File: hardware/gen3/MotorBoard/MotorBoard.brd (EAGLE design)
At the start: 140 x 100 mm, 273 parts, among them M10O1 TEST_PT, M1O2 TEST_PT, M1O3 TEST_PT, M2O1 TEST_PT, M2O2 TEST_PT, M2O3 TEST_PT, M3O1 TEST_PT, M3O2 TEST_PT, M3O3 TEST_PT, M4O1 TEST_PT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

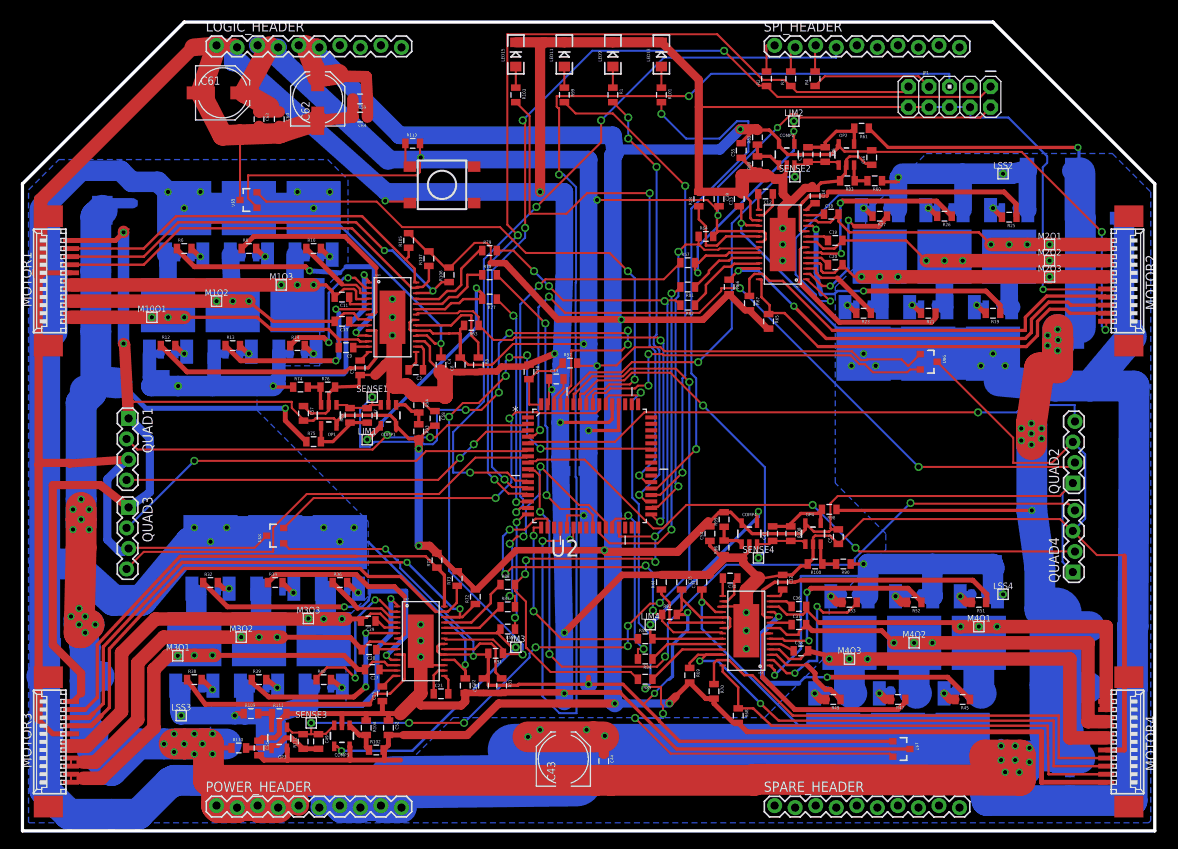
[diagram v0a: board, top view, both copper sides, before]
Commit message: DRC fixes for mtor
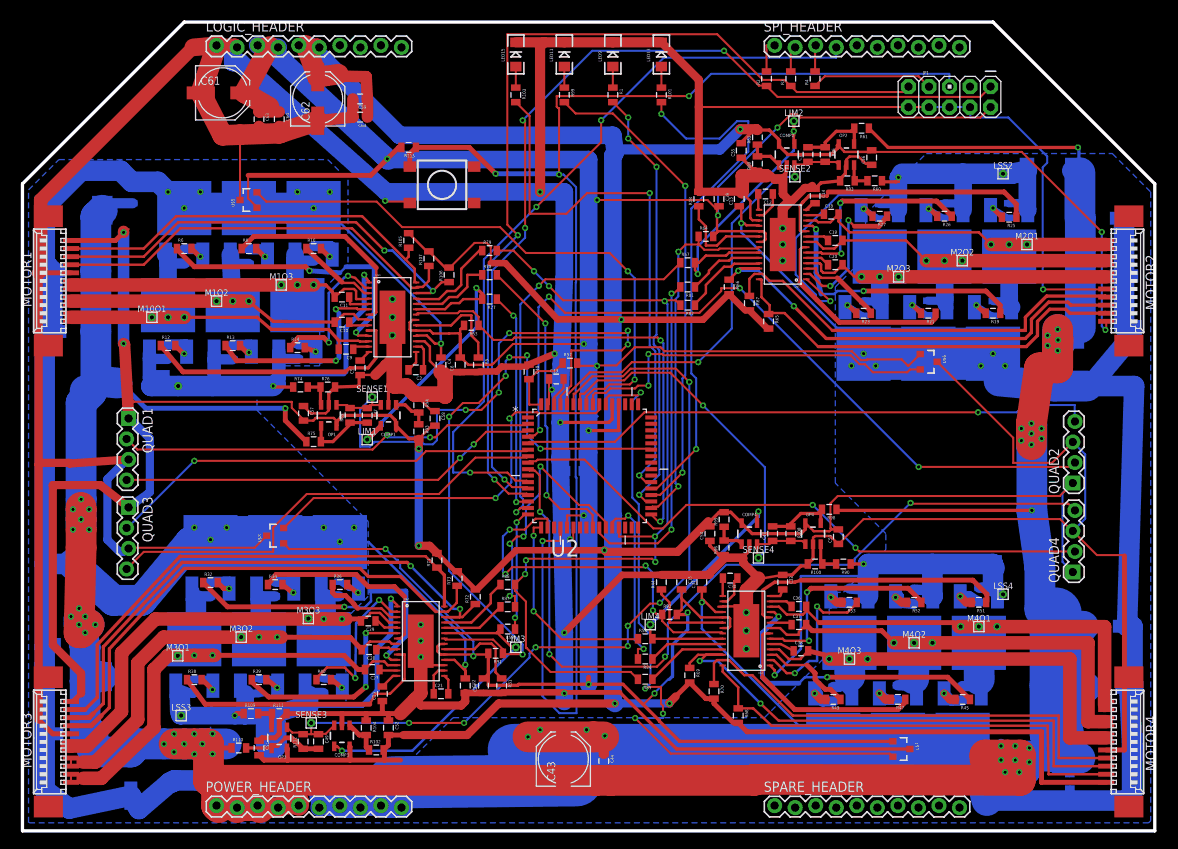
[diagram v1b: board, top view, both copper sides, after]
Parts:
- moved M2O3 18.7 mm to (108.3, 68.5)
- moved M2O2 10.8 mm to (116.2, 70.5)
- moved C50 3.32 mm to (13.4, 7.05)
- moved M2O1 2.79 mm to (124.2, 72.5)
- moved C25 0.75 mm to (133.9, 25.3)
- moved R113 0.71 mm to (47.8, 84.5), turned to 180 degrees
- moved D2 0.65 mm to (130.1, 13.5)
- moved R11 0.40 mm to (36.0, 71.4), turned to 270 degrees
- moved R20 0.40 mm to (120.0, 64.6), turned to 90 degrees
- moved R24 0.40 mm to (104.0, 64.6), turned to 90 degrees
- moved R30 0.40 mm to (106.0, 76.6), turned to 90 degrees
- moved R22 0.35 mm to (112.0, 64.7), turned to 90 degrees
- moved R50 0.35 mm to (100.2, 16.9), turned to 90 degrees
- moved C42 0.35 mm to (134.2, 17.8)
- moved D3 0.30 mm to (9.80, 15.9)
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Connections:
- removed net RESET1: R113.1, S1.A2
- net RESET: now also R113.1, S1.A2
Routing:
- net RESET: track 157.2 -> 179.5 mm, vias 3 -> 4
- net 12VGND: track 474.6 -> 487.3 mm, vias 22 -> 41
- net 12V: track 620.0 -> 629.8 mm, vias 9 -> 22
- net O2: track 67.8 -> 72.4 mm
- net 3.3V: track 451.7 -> 447.3 mm
- net O4: track 58.2 -> 61.7 mm
- net N$57: track 4.82 -> 8.30 mm
- net RESET1: track 3.42 -> 0.00 mm
- net O1: track 67.3 -> 70.4 mm
- net N$79: track 4.12 -> 6.61 mm
- net O3: track 57.8 -> 60.2 mm
- net N$80: track 4.12 -> 6.36 mm
- net M4O1: track 66.8 -> 68.7 mm
- net N$54: track 4.76 -> 6.51 mm
- net N$55: track 3.89 -> 5.38 mm
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
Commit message: fixed all DRC. vias in pads are ok, right?
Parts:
- moved LSS4 5.66 mm to (117.2, 33.2)
- renumbered M10O1 to M1O1
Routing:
- net O4: track 61.7 -> 66.3 mm
- net 12V: track 629.8 -> 634.0 mm, vias 22 -> 26
- net GND: track 857.2 -> 859.4 mm, vias 16 -> 17
- net 12VGND: track 487.3 -> 489.1 mm, vias 41 -> 44
- net RESET: track 179.5 -> 181.1 mm
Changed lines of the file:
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@@
 <setting verticaltext="up"/>
 </settings>
-<grid distance="0.05" unitdist="mm" unit="mm" style="lines" multiple="1" display="yes" altdistance="0.005" altunitdist="inch" altunit="inch"/>
+<grid distance="1" unitdist="mm" unit="mm" style="lines" multiple="1" display="yes" altdistance="0.005" altunitdist="inch" altunit="inch"/>
 <layers>
-<layer number="1" name="Top" color="4" fill="1" visible="no" active="yes"/>
+<layer number="1" name="Top" color="4" fill="1" visible="yes" active="yes"/>
 <layer number="2" name="Route2" color="1" fill="3" visible="no" active="no"/>
 <layer number="3" name="Route3" color="4" fill="3" visible="no" active="no"/>
@@
 </class>
 </classes>
-<designrules name="default">
+<designrules name="default *">
 <description language="de">&lt;b&gt;EAGLE Design Rules&lt;/b&gt;
 &lt;p&gt;
@@
 <param name="mdSmdStop" value="0mil"/>
 <param name="msWidth" value="10mil"/>
-<param name="msDrill" value="24mil"/>
+<param name="msDrill" value="15mil"/>
 <param name="msMicroVia" value="9.99mm"/>
 <param name="msBlindViaRatio" value="0.5"/>
@@
 <element name="LSS1" library="gen3" package="TESTING_PT" value="TEST_PT" x="19.25" y="55" rot="MR0"/>
 <element name="LSS2" library="gen3" package="TESTING_PT" value="TEST_PT" x="121.25" y="81.25"/>
-<element name="LSS4" library="gen3" package="TESTING_PT" value="TEST_PT" x="121.25" y="29.25"/>
+<element name="LSS4" library="gen3" package="TESTING_PT" value="TEST_PT" x="117.25" y="33.25"/>
 <element name="LSS3" library="gen3" package="TESTING_PT" value="TEST_PT" x="19.625" y="14.25"/>
 <element name="M3O3" library="gen3" package="TESTING_PT" value="TEST_PT" x="35.35" y="26.25"/>
@@
 <element name="M2O2" library="gen3" package="TESTING_PT" value="TEST_PT" x="116.205" y="70.5"/>
 <element name="M2O3" library="gen3" package="TESTING_PT" value="TEST_PT" x="108.331" y="68.5"/>
-<element name="M10O1" library="gen3" package="TESTING_PT" value="TEST_PT" x="16" y="63.5"/>
+<element name="M1O1" library="gen3" package="TESTING_PT" value="TEST_PT" x="16" y="63.5"/>
 <element name="M1O2" library="gen3" package="TESTING_PT" value="TEST_PT" x="24" y="65.5"/>
 <element name="M1O3" library="gen3" package="TESTING_PT" value="TEST_PT" x="32" y="67.5"/>
@@
 <wire x1="21.123" y1="96.873" x2="2.25" y2="78" width="1.6764" layer="1"/>
 <wire x1="2.25" y1="78" x2="2.25" y2="69.25" width="1.6764" layer="1"/>
-<wire x1="2.25" y1="69.25" x2="2" y2="69" width="1.6764" layer="1"/>
+<wire x1="2.25" y1="69.25" x2="2" y2="69" width="1.4224" layer="1"/>
 <wire x1="49.25" y1="23.455" x2="49.25" y2="21.5" width="1.6764" layer="1"/>
 <wire x1="49.25" y1="21.5" x2="49.25" y2="20.5" width="1.6764" layer="1"/>
@@
 <wire x1="26.55" y1="96.9" x2="26.54" y2="96.873" width="0.254" layer="16"/>
 <wire x1="26.55" y1="96.9" x2="26" y2="96.333" width="0.254" layer="16"/>
+<via x="45.75" y="65.75" extent="1-16" drill="0.508"/>
+<wire x1="45.75" y1="65.75" x2="45.75" y2="63.5" width="1.27" layer="1"/>
 </signal>
 <signal name="3.3V">
@@
 <wire x1="47.9" y1="82.15" x2="47.9" y2="83.75" width="0.609" layer="1"/>
 <wire x1="47.9" y1="83.75" x2="48.65" y2="84.5" width="0.609" layer="1"/>
-<wire x1="48.65" y1="84.5" x2="55.25" y2="84.5" width="0.609" layer="1"/>
-<wire x1="55.25" y1="84.5" x2="58.5" y2="81.25" width="0.609" layer="1"/>
+<wire x1="48.65" y1="84.5" x2="58.25" y2="84.5" width="0.609" layer="1"/>
+<wire x1="58.25" y1="84.5" x2="58.5" y2="81.25" width="0.609" layer="1"/>
 <via x="58.5" y="81.25" extent="1-16" drill="0.381" diameter="0.508"/>
 <wire x1="58.5" y1="81.25" x2="66.25" y2="81.25" width="0.609" layer="16"/>
@@
 <via x="69.75" y="12.5" extent="1-16" drill="0.381" diameter="0.508"/>
 <via x="72" y="11.75" extent="1-16" drill="0.381" diameter="0.508"/>
-<wire x1="20" y1="77" x2="22" y2="79" width="0" layer="19" extent="16-16"/>
-<wire x1="72" y1="11.75" x2="71.875" y2="11.625" width="0" layer="19" extent="1-1"/>
+<via x="102.5" y="57.5" extent="1-16" drill="0.381"/>
+<via x="105.5" y="57.5" extent="1-16" drill="0.381"/>
+<wire x1="105.5" y1="57.5" x2="104" y2="59" width="1.27" layer="16"/>
+<wire x1="102.5" y1="57.5" x2="104" y2="59" width="1.27" layer="16"/>
+<via x="118.5" y="57.5" extent="1-16" drill="0.381"/>
+<via x="121.5" y="57.5" extent="1-16" drill="0.381"/>
+<wire x1="120.5" y1="58.5" x2="121.5" y2="57.5" width="0" layer="19" extent="16-16"/>
 <wire x1="18" y1="79" x2="16.75" y2="80.25" width="0" layer="19" extent="16-16"/>
+<wire x1="118.5" y1="57.5" x2="120" y2="59" width="0" layer="19" extent="16-16"/>
 <wire x1="41" y1="37.5" x2="39.25" y2="35.75" width="0" layer="19" extent="1-1"/>
 <wire x1="37.25" y1="37.5" x2="39.25" y2="35.75" width="0" layer="19" extent="1-1"/>
+<wire x1="22" y1="79" x2="20" y2="77" width="0" layer="19" extent="16-16"/>
 </signal>
 <signal name="12VGND">
@@
 <wire x1="31.874" y1="3.127" x2="31.62" y2="2.873" width="2.1844" layer="1"/>
 <wire x1="31.62" y1="2.873" x2="29.334" y2="2.873" width="2.54" layer="1"/>
-<wire x1="29.334" y1="2.873" x2="29.08" y2="3.127" width="3.81" layer="1"/>
-<wire x1="29.08" y1="3.127" x2="26.794" y2="3.127" width="3.81" layer="1"/>
-<wire x1="26.794" y1="3.127" x2="26.54" y2="2.873" width="3.81" layer="1"/>
+<wire x1="29.334" y1="2.873" x2="29.08" y2="3.127" width="2.54" layer="1"/>
+<wire x1="29.08" y1="3.127" x2="26.794" y2="3.127" width="2.54" layer="1"/>
+<wire x1="26.794" y1="3.127" x2="26.54" y2="2.873" width="2.54" layer="1"/>
 <wire x1="26.54" y1="2.873" x2="24.254" y2="2.873" width="2.54" layer="1"/>
-<wire x1="24.254" y1="2.873" x2="24" y2="3.127" width="3.81" layer="1"/>
-<wire x1="24" y1="3.127" x2="24" y2="6" width="3.81" layer="1"/>
+<wire x1="24.254" y1="2.873" x2="24" y2="3.127" width="2.54" layer="1"/>
+<wire x1="24" y1="3.127" x2="24" y2="6" width="2.54" layer="1"/>
 <wire x1="24" y1="6" x2="23" y2="6.25" width="3.81" layer="1"/>
 <wire x1="23" y1="6.25" x2="70.875" y2="6.25" width="3.81" layer="1"/>
@@
 <wire x1="128" y1="57.25" x2="128" y2="59.375" width="3.81" layer="1"/>
 <via x="128" y="62" extent="1-16" drill="0.381"/>
-<wire x1="128" y1="59.375" x2="128" y2="62" width="3.81" layer="1"/>
+<wire x1="128" y1="60.075" x2="128" y2="62" width="3.81" layer="1"/>
 <wire x1="128" y1="62" x2="128" y2="59.375" width="3.81" layer="16"/>
 <via x="128" y="59.375" extent="1-16" drill="0.381"/>
-<wire x1="128" y1="59.375" x2="128" y2="60.075" width="3.81" layer="1"/>
+<wire x1="128" y1="59.375" x2="128" y2="60" width="3.81" layer="1"/>
+<wire x1="128" y1="60" x2="128" y2="60.075" width="3.81" layer="1"/>
 <wire x1="128" y1="60.075" x2="128.05" y2="60.7" width="3.81" layer="1"/>
 <via x="128.05" y="60.7" extent="1-16" drill="0.381"/>
@@
 <wire x1="123.5" y1="48.25" x2="124.25" y2="48.25" width="0.3048" layer="1"/>
 <wire x1="124.25" y1="48.25" x2="124.75" y2="47.75" width="0.3048" layer="1"/>
-<wire x1="125.5" y1="9.25" x2="124.5" y2="10.25" width="0" layer="19" extent="16-16"/>
+<via x="126" y="49.75" extent="1-16" drill="0.381" diameter="0.508"/>
+<via x="126.75" y="60" extent="1-16" drill="0.381" diameter="0.508"/>
+<via x="126.75" y="61.25" extent="1-16" drill="0.381" diameter="0.508"/>
+<wire x1="126.75" y1="60" x2="128" y2="60" width="1.27" layer="1"/>
 <wire x1="121.5" y1="7.25" x2="121.5" y2="6.75" width="0" layer="19" extent="16-16"/>
 <wire x1="122.75" y1="8.75" x2="122.5" y2="9.25" width="0" layer="19" extent="16-16"/>
 <wire x1="123.25" y1="7.25" x2="123.375" y2="7.875" width="0" layer="19" extent="16-16"/>
+<wire x1="126" y1="49.75" x2="126" y2="48.5" width="0" layer="19" extent="1-1"/>
 <wire x1="124.5" y1="8.5" x2="125.5" y2="9.25" width="0" layer="19" extent="16-16"/>
 <wire x1="122.75" y1="10.5" x2="122.5" y2="9.25" width="0" layer="19" extent="16-16"/>
+<wire x1="124.5" y1="10.25" x2="125.5" y2="9.25" width="0" layer="19" extent="16-16"/>
+<wire x1="126.75" y1="61.25" x2="126.75" y2="60" width="1.27" layer="1"/>
 </signal>
 <signal name="5V">
@@
 <wire x1="30.75" y1="62" x2="37.875" y2="62" width="0.4064" layer="1"/>
 <wire x1="37.875" y1="62" x2="39.125" y2="60.6" width="0.4064" layer="1"/>
-<contactref element="M10O1" pad="P$1"/>
+<contactref element="M1O1" pad="P$1"/>
 <wire x1="6" y1="63" x2="12.5" y2="63" width="0.4064" layer="1"/>
 <wire x1="12.5" y1="63" x2="16" y2="63.5" width="0.4064" layer="1"/>
@@
 <wire x1="120.2" y1="32.5" x2="120" y2="32.5" width="2.54" layer="16"/>
 <wire x1="120" y1="32.5" x2="120" y2="33" width="2.54" layer="16"/>
-<wire x1="121.25" y1="29.25" x2="120.55" y2="29" width="0.254" layer="16"/>
+<wire x1="117.25" y1="33.25" x2="120.55" y2="29" width="0.254" layer="16"/>
 </signal>
 <signal name="O3">
@@
 <signal name="N$100">
 </signal>
-<signal name="N$103">
-<via x="121.5" y="57.5" extent="1-16" drill="0.381"/>
-</signal>
-<signal name="N$108">
-<via x="118.5" y="57.5" extent="1-16" drill="0.381"/>
-</signal>
-<signal name="N$109">
-<via x="105.5" y="57.5" extent="1-16" drill="0.381"/>
-</signal>
-<signal name="N$111">
-<via x="102.5" y="57.5" extent="1-16" drill="0.381"/>
-</signal>
-<signal name="N$122">
-<via x="45.75" y="65.75" extent="1-16" drill="0.508"/>
-</signal>
 <signal name="N$123">
 <via x="94" y="70.5" extent="1-16" drill="0.508"/>
@@
 <via x="89.5" y="22.5" extent="1-16" drill="0.508"/>
 </signal>
-<signal name="N$145">
-<via x="126" y="49.75" extent="1-16" drill="0.381" diameter="0.508"/>
-</signal>
-<signal name="N$149">
-<via x="126.75" y="61.25" extent="1-16" drill="0.381" diameter="0.508"/>
-</signal>
-<signal name="N$150">
-<via x="126.75" y="60" extent="1-16" drill="0.381" diameter="0.508"/>
-</signal>
 </signals>
+<errors>
+</errors>
 </board>
 </drawing>

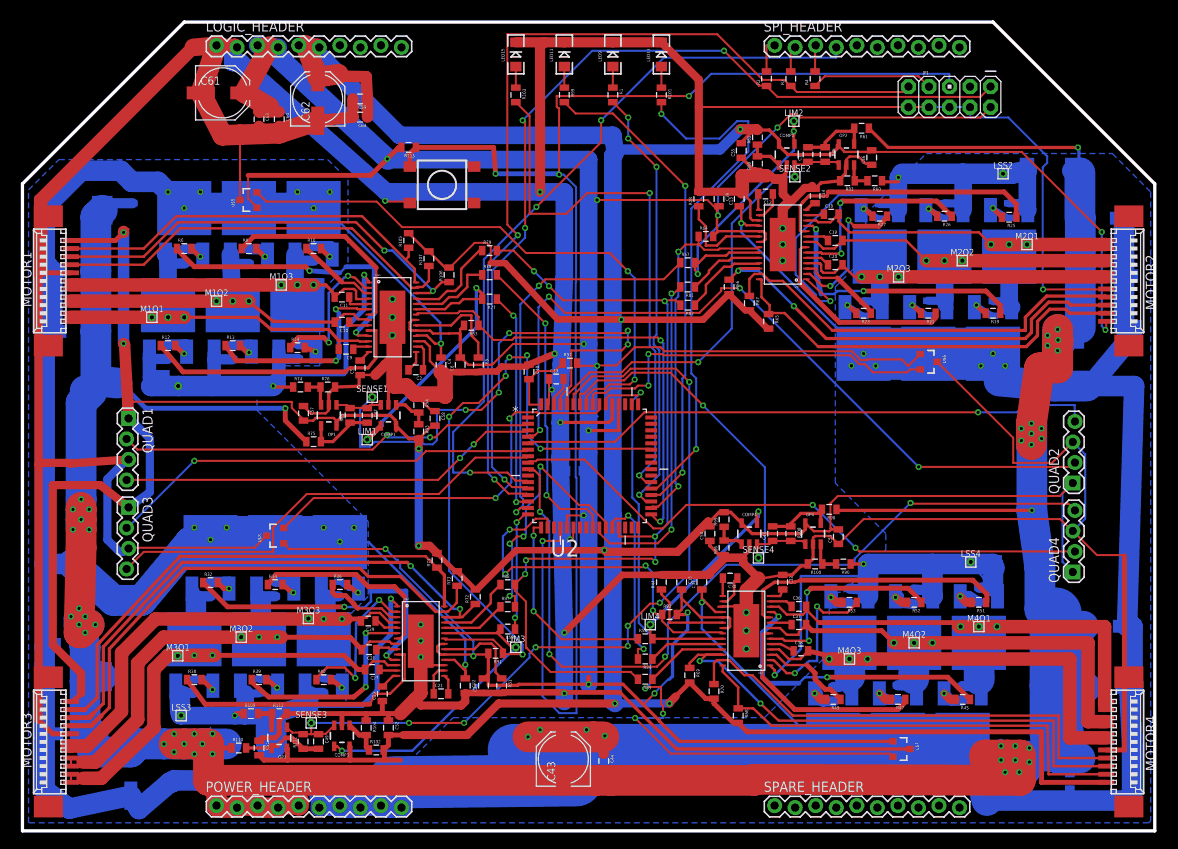
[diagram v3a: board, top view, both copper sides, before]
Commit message: wider traces on motor
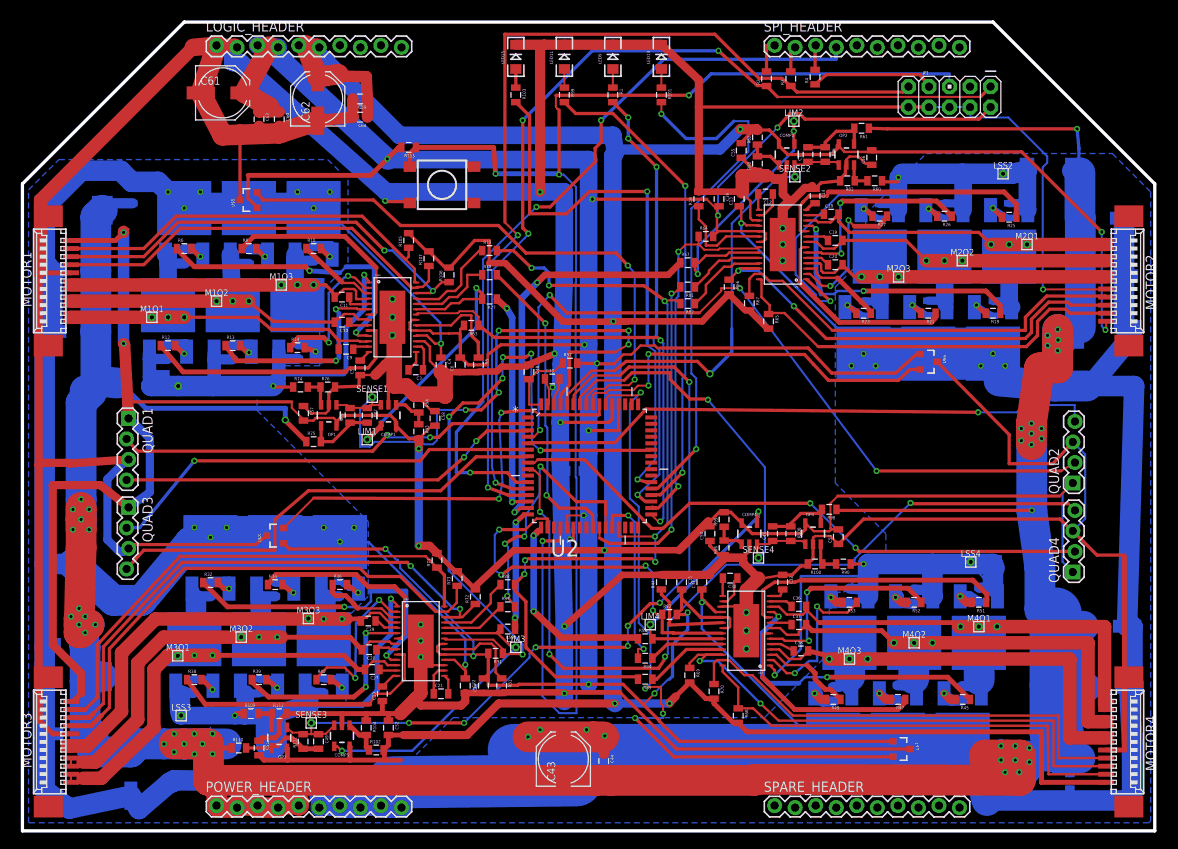
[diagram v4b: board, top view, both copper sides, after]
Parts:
- moved C33 0.50 mm to (65.5, 55.9)
- moved LED11 0.30 mm to (67.0, 95.7)
- moved LED13 0.30 mm to (79.0, 95.7)
- moved LED15 0.30 mm to (61.0, 95.7)
- moved LED9 0.30 mm to (73.0, 95.7)
- moved R4 0.20 mm to (98.0, 93.2)
- moved R82 0.20 mm to (82.2, 65.2)
- moved R84 0.10 mm to (77.0, 21.4)
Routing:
- net 5V: track 651.1 -> 654.6 mm
- net SENSE2: track 55.4 -> 58.4 mm
- net FAULT4: track 46.3 -> 49.1 mm
- net M2QA: track 95.7 -> 98.2 mm
- net TSENSE3: track 50.8 -> 52.5 mm
- net DIR3: track 31.9 -> 33.2 mm
- net MISO: track 115.2 -> 116.5 mm
- net 12VGND: track 489.1 -> 490.3 mm
- net FAULT3: track 83.8 -> 85.0 mm
- net SENSE1: track 74.9 -> 76.0 mm
- net TSENSE2: track 47.0 -> 47.9 mm
- net 3.3V: track 447.3 -> 448.1 mm
- net SENSE4: track 49.8 -> 50.5 mm
- net M3QA: track 53.7 -> 54.3 mm
- net GLED4: track 68.3 -> 68.9 mm
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
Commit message: added logos. generated gerbers
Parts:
- added U$9: LOGO, gen3:LOGO
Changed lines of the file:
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@@
 <layer number="56" name="wert" color="7" fill="1" visible="no" active="no"/>
 <layer number="57" name="tCAD" color="7" fill="1" visible="no" active="no"/>
+<layer number="59" name="tCarbon" color="7" fill="1" visible="no" active="no"/>
+<layer number="60" name="bCarbon" color="7" fill="1" visible="no" active="no"/>
 <layer number="90" name="Modules" color="5" fill="1" visible="no" active="no"/>
 <layer number="91" name="Nets" color="2" fill="1" visible="no" active="no"/>
@@
 <layer number="127" name="_tValues" color="7" fill="1" visible="yes" active="yes"/>
 <layer number="128" name="_bValues" color="7" fill="1" visible="yes" active="yes"/>
+<layer number="129" name="Mask" color="7" fill="1" visible="yes" active="yes"/>
 <layer number="131" name="tAdjust" color="7" fill="1" visible="yes" active="yes"/>
 <layer number="132" name="bAdjust" color="7" fill="1" visible="yes" active="yes"/>
@@
 <layer number="251" name="SMDround" color="12" fill="11" visible="no" active="no"/>
 <layer number="254" name="cooling" color="7" fill="1" visible="yes" active="yes"/>
+<layer number="255" name="routoute" color="7" fill="1" visible="yes" active="yes"/>
 </layers>
 <board>
@@
 <element name="C45" library="SparkFun-Capacitors" package="0805" value="1uF" x="68.25" y="44.5" rot="MR0"/>
 <element name="C46" library="SparkFun-Capacitors" package="0805" value=".01uF" x="68.25" y="46.5" rot="MR0"/>
+<element name="U$9" library="gen3" package="LOGO" value="LOGO" x="86" y="44.7"/>
 </elements>
 <signals>
@@
 </board>
 </drawing>
+<compatibility>
+<note version="6.3" minversion="6.2.2" severity="warning">
+Since Version 6.2.2 text objects can contain more than one line,
+which will not be processed correctly with this version.
+</note>
+</compatibility>
 </eagle>
